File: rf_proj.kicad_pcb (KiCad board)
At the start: 2 copper layers, 85 parts, among them IC1 ATMEGA328P-A, P2 USB_OTG, P3 BNC, Q1 2N3904, SW1 SW_PUSH, U1 Si5351A_3, U2 CH340, U3 74AC74, U4 74CBTLV3253, U5 TLV2464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

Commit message: Layout verbessert.
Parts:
- removed Y1: 25MHZ, Crystals:Crystal_HC49-SD_SMD
- removed Y2: 12MHZ, Crystals:Crystal_HC49-SD_SMD
- removed Y3: 16MHZ, Crystals:Crystal_HC49-SD_SMD
- added C30: C_Small, Capacitors_SMD:C_0603_HandSoldering, F.Cu at (50.2, 96.5)
- added C31: C_Small, Capacitors_SMD:C_0603_HandSoldering, F.Cu at (50.2, 98.4)
- added C32: C_Small, Capacitors_SMD:C_0603_HandSoldering, F.Cu at (50.2, 102.2)
- added C33: C_Small, Capacitors_SMD:C_0603_HandSoldering, F.Cu at (50.2, 100.3)
- added C35: 10uF, Capacitors_SMD:C_0805_HandSoldering, F.Cu at (140.9, 113.8)
- added C36: 0.1uF, Capacitors_SMD:C_0603_HandSoldering, F.Cu at (145.8, 113.6)
- added CON1: AVR-ISP-6, Pin_Headers:Pin_Header_Straight_2x03, F.Cu at (268.0, 89.5)
- added D1: Led_Small, LEDs:LED_0603, F.Cu at (247.8, 84.5)
- added D2: Led_Small, LEDs:LED_0603, F.Cu at (247.8, 86.4)
- added D3: Led_Small, LEDs:LED_0603, F.Cu at (247.8, 88.3)
- added D4: Led_Small, LEDs:LED_0603, F.Cu at (247.8, 90.2)
- added D5: Led_Small, LEDs:LED_0603, F.Cu at (304.9, 66.7)
- added L8: INDUCTOR, Choke_SMD:Choke_SMD_1206_Handsoldering, F.Cu at (134.4, 114.3)
- added L9: INDUCTOR, Choke_SMD:Choke_SMD_1206_Handsoldering, F.Cu at (134.4, 121.4)
- added R32: 470, Resistors_SMD:R_0603_HandSoldering, F.Cu at (251.3, 84.5)
- added R33: 470, Resistors_SMD:R_0603_HandSoldering, F.Cu at (251.3, 86.4)
- added R34: 470, Resistors_SMD:R_0603_HandSoldering, F.Cu at (251.3, 88.3)
- added R35: 470, Resistors_SMD:R_0603_HandSoldering, F.Cu at (251.3, 90.2)
- added R36: 470, Resistors_SMD:R_0603_HandSoldering, F.Cu at (304.8, 69.2)
- added R37: 390, Resistors_SMD:R_0603_HandSoldering, F.Cu at (54.8, 103.5)
- added R38: R, Resistors_SMD:R_0603_HandSoldering, F.Cu at (140.6, 119.9)
- added T1: TRANSFO, rf-proj:RF-ProjTransformer, F.Cu at (34.9, 73.7)
- added X3: 25MHz, Crystals:Crystal_SMD_2520_4Pads, F.Cu at (214.3, 37.0)
- C34: footprint Resistors_SMD:R_0603_HandSoldering -> Capacitors_SMD:C_0603_HandSoldering
- moved X1 225.9 mm to (299.1, 84.5)
- moved SW1 176.1 mm to (315.0, 72.4)
- moved U2 176.1 mm to (297.2, 76.2)
- moved P2 176.1 mm to (297.8, 67.9)
- moved X2 163.6 mm to (247.0, 78.7)
- moved R6 133.7 mm to (23.8, 89.3), turned to 180 degrees
- moved U7 132.2 mm to (195.6, 128.5)
- moved C15 130.9 mm to (28.9, 91.2), turned to 90 degrees
- moved C11 126.6 mm to (252.7, 78.4), turned to 270 degrees
- moved IC1 125.0 mm to (260.4, 76.4)
- moved R5 122.6 mm to (28.9, 95.7), turned to 270 degrees
- moved R7 119.1 mm to (30.8, 95.7), turned to 90 degrees
- moved R4 115.8 mm to (28.4, 88.0), turned to 180 degrees
- moved R8 114.9 mm to (23.2, 92.9), turned to 90 degrees
- moved C20 106.4 mm to (30.8, 91.2), turned to 270 degrees
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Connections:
- C10 pad 2: GND -> GNDA
- C18 pad 2: GND -> GNDA
- C22 pad 2: GND -> GNDA
- C27 pad 2: GND -> GNDA
- C28 pad 2: GND -> GNDA
- C6 pad 2: GND -> GNDA
- C7 pad 2: GND -> GNDA
- C9 pad 2: GND -> GNDA
- R22 pad 1: GND -> GNDA
- R30 pad 1: GND -> GNDA
- R6 pad 2: GND -> GNDA
- R8 pad 2: GND -> GNDA
- U4 pad 8: GND -> GNDA
- U4 pad 9: Net-(U4-Pad9) -> GNDA
- U5 pad 11: GND -> GNDA
- U5 pad 12: /IN_D -> (no net)
- U5 pad 13: Net-(R19-Pad1) -> (no net)
- U5 pad 14: Net-(R24-Pad1) -> (no net)
- U6 pad 11: GND -> GNDA
- U6 pad 12: (no net) -> Net-(C24-Pad1)
- U6 pad 13: (no net) -> /V_REF
- U6 pad 14: (no net) -> /V_REF
- U6 pad 5: Net-(C24-Pad1) -> /IN_D
- U6 pad 6: /V_REF -> Net-(R19-Pad1)
- U6 pad 7: /V_REF -> Net-(R24-Pad1)
- U7 pad 1: GND -> GNDA
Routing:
- net Net-(L5-Pad1): track 0.00 -> 12.4 mm
- net Net-(R27-Pad1): track 0.00 -> 9.21 mm
- net Net-(C15-Pad1): track 0.00 -> 8.52 mm
- net Net-(R19-Pad1): track 0.00 -> 6.91 mm
- net Net-(R19-Pad2): track 0.00 -> 6.77 mm
- net Net-(R23-Pad1): track 0.00 -> 4.66 mm
- net Net-(C29-Pad1): track 0.00 -> 4.21 mm
- net Net-(R26-Pad1): track 0.00 -> 3.97 mm
- net /V_REF: track 0.00 -> 2.94 mm
- net GNDA: track 0.00 -> 2.73 mm
- net Net-(C15-Pad2): track 0.00 -> 2.49 mm
- net Net-(Q1-Pad1): track 0.00 -> 2.25 mm
- net Net-(R24-Pad1): track 0.00 -> 2.15 mm

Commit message: Routing und Fehlerkorrekturen im Schaltplan
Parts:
- added C37: 10uF, Capacitors_SMD:C_0805_HandSoldering, F.Cu at (102.2, 116.8)
- added C38: 0.1uF, Capacitors_SMD:C_0603_HandSoldering, F.Cu at (99.1, 118.1)
- added C39: 10uF, Capacitors_SMD:C_0805_HandSoldering, F.Cu at (128.9, 110.5)
- added C40: 0.1uF, Capacitors_SMD:C_0603_HandSoldering, F.Cu at (127.6, 107.3)
- added C41: 1uF, Capacitors_SMD:C_0603_HandSoldering, F.Cu at (172.1, 89.2)
- added J1: JACK_TRS_6PINS, Connect:PINHEAD1-6, F.Cu at (141.0, 108.0)
- added L10: INDUCTOR, rf-proj:L_0805_HandSoldering, F.Cu at (102.2, 119.4)
- added L11: INDUCTOR, rf-proj:L_0805_HandSoldering, F.Cu at (126.4, 110.5)
- added R39: R, Resistors_SMD:R_0603_HandSoldering, F.Cu at (102.2, 121.3)
- added R40: R, Resistors_SMD:R_0603_HandSoldering, F.Cu at (124.5, 110.5)
- L1, L2, L3, L4, L5, L6, L7, L8, L9: footprint Choke_SMD:Choke_SMD_1206_Handsoldering -> rf-proj:L_0805_HandSoldering
- moved SW1 146.9 mm to (177.8, 125.1), turned to 180 degrees
- moved X1 135.3 mm to (163.8, 81.2), turned to 270 degrees
- moved U2 125.2 mm to (172.1, 80.6), turned to 180 degrees
- moved R36 124.1 mm to (180.8, 74.3)
- moved D5 124.1 mm to (181.0, 72.4)
- moved L7 121.1 mm to (184.8, 154.3), turned to 180 degrees
- moved P2 118.1 mm to (180.4, 80.0), turned to 90 degrees
- moved R20 108.9 mm to (108.6, 119.4), turned to 180 degrees
- moved U3 99.6 mm to (155.2, 125.8)
- moved U1 99.5 mm to (162.6, 125.4), turned to 180 degrees
- moved X3 99.1 mm to (168.9, 125.1)
- moved R14 96.4 mm to (116.2, 116.2), turned to 270 degrees
- moved C27 93.3 mm to (197.5, 149.2)
- moved C11 93.2 mm to (160.7, 92.7), turned to 0 degrees
- moved IC1 92.0 mm to (170.8, 97.2)
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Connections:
- C16 pad 2: GND -> GNDA
- C18 pad 1: /3.3A -> Net-(C18-Pad1)
- C19 pad 2: GND -> GNDA
- C22 pad 1: /3.3A -> Net-(C18-Pad1)
- C24 pad 2: GND -> GNDA
- C34 pad 2: GND -> GNDA
- P2 pad 6: Net-(P2-Pad6) -> GND
- R21 pad 1: GND -> GNDA
- R7 pad 1: /3.3A -> Net-(C38-Pad1)
- U2 pad 13: Net-(U2-Pad13) -> /DTR
- U4 pad 1: Net-(U4-Pad1) -> GNDA
- U4 pad 15: Net-(U4-Pad15) -> Net-(C19-Pad1)
- U5 pad 12: (no net) -> Net-(C24-Pad1)
- U5 pad 13: (no net) -> /V_REF
- U5 pad 14: (no net) -> /V_REF
- U5 pad 4: /3.3A -> Net-(C18-Pad1)
- U6 pad 12: Net-(C24-Pad1) -> GNDA
- U6 pad 13: /V_REF -> GNDA
- U6 pad 14: /V_REF -> Net-(U6-Pad14)
- U6 pad 4: /3.3A -> Net-(C18-Pad1)
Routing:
- net GNDA: track 2.73 -> 77.8 mm, vias 0 -> 5
- net GND: track 0.00 -> 69.7 mm
- net /S0: track 0.00 -> 55.3 mm, vias 0 -> 3
- net /S1: track 0.00 -> 50.9 mm, vias 0 -> 2
- net /RESET: track 0.00 -> 41.3 mm
- net /S_Mixer: track 0.00 -> 41.2 mm, vias 0 -> 3
- net /3.3A: track 0.00 -> 35.8 mm, vias 0 -> 2
- net Net-(C18-Pad1): track 0.00 -> 35.4 mm, vias 0 -> 5
- net Net-(C38-Pad1): track 0.00 -> 30.9 mm
- net +3V3: track 0.00 -> 30.4 mm
- net /V_REF: track 2.94 -> 29.2 mm
- net Net-(C24-Pad1): track 0.00 -> 22.9 mm, vias 0 -> 2
- net Net-(C2-Pad1): track 0.00 -> 22.1 mm
- net /IN_C: track 0.00 -> 21.1 mm
- net /IN_D: track 0.00 -> 20.8 mm
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- added copper zone on B.Cu, net GND
- added copper zone on F.Cu, net GND
- added copper zone on B.Cu, net GNDA
- added copper zone on F.Cu, net GNDA
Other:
- net class Default: via_dia 0.8 -> 1
- rule trace_min: 0.2 -> 0.25
- rule via_min_drill: 0.3 -> 0.4
- rule via_min_size: 0.4 -> 1

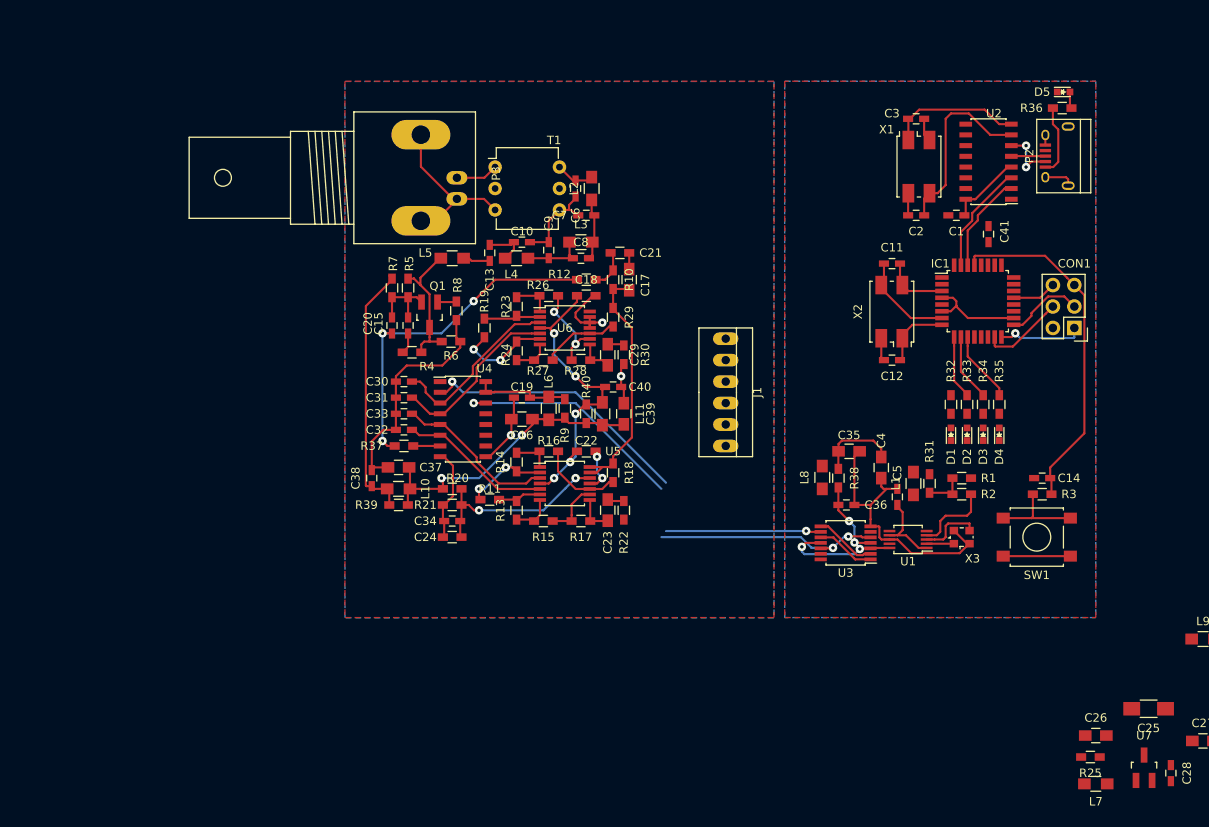
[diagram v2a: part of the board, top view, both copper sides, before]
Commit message: Footprints angepasst und Layout bearbeitet
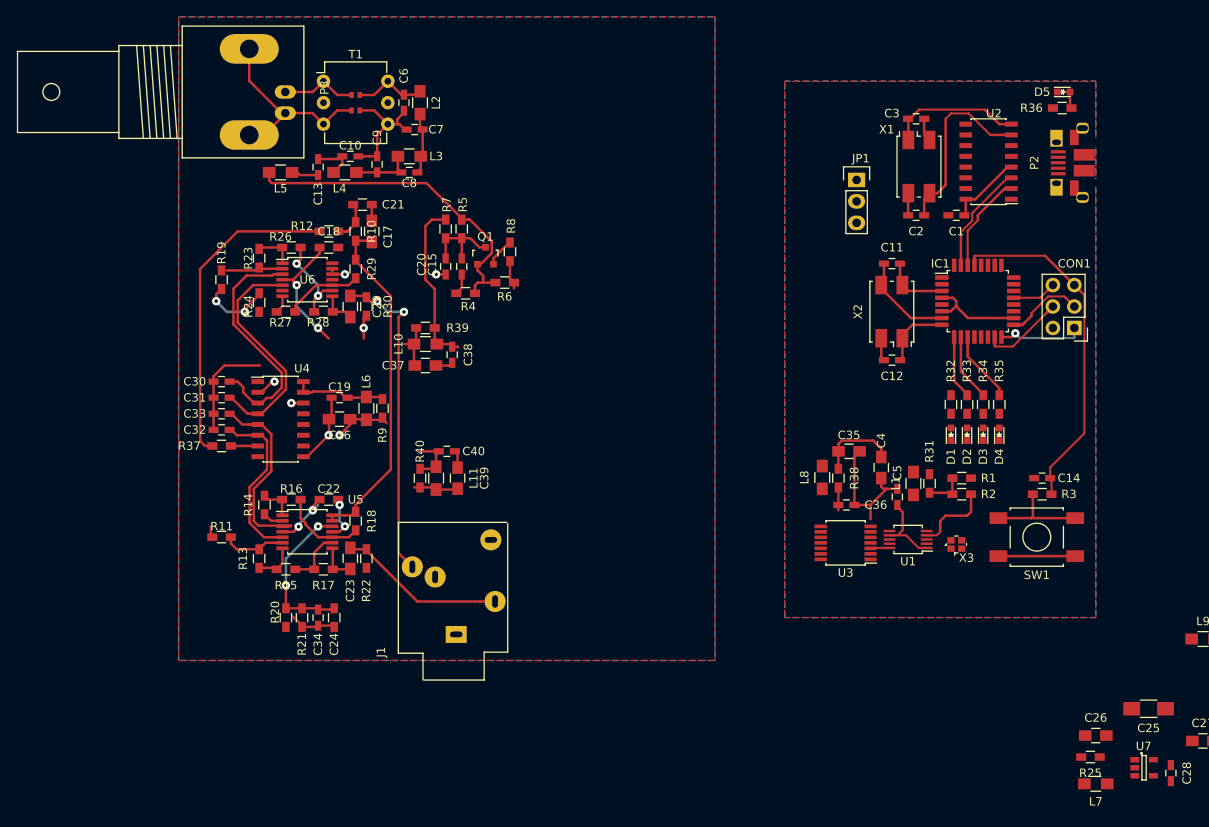
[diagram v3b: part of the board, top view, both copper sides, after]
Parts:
- removed C41: 1uF, Capacitors_SMD:C_0603_HandSoldering
- added JP1: JUMPER3, Pin_Headers:Pin_Header_Straight_1x03, F.Cu at (156.5, 82.8)
- J1: value JACK_TRS_6PINS -> EBS_35; footprint Connect:PINHEAD1-6 -> rf-proj:EBS_35
- P2: footprint Connect:USB_Micro-B -> rf-proj:USB_Micro-B
- Q1: value 2N3904 -> BC849; footprint TO_SOT_Packages_SMD:SOT-23_Handsoldering -> TO_SOT_Packages_SMD:SOT-23
- SW1: footprint Buttons_Switches_SMD:SW_SPST_B3S-1000 -> rf-proj:TASTER_9315
- U7: value AP1117D33 -> MIC5504-3.3; footprint TO_SOT_Packages_SMD:SOT-23_Handsoldering -> TO_SOT_Packages_SMD:SOT-23-5
- X3: footprint Crystals:Crystal_SMD_2520_4Pads -> rf-proj:Crystal_SMD_2016_4Pads
- moved J1 46.7 mm to (109.1, 142.0), turned to 90 degrees
- moved R11 32.1 mm to (81.3, 125.1)
- moved R19 31.6 mm to (81.3, 94.6)
- moved C21 31.0 mm to (98.0, 85.7)
- moved C23 31.0 mm to (96.5, 127.6)
- moved C29 31.0 mm to (96.5, 97.8)
- moved R10 31.0 mm to (97.2, 88.9)
- moved R13 31.0 mm to (85.7, 127.6)
- moved R16 31.0 mm to (89.5, 120.7)
- moved R17 31.0 mm to (93.3, 128.9)
- moved R18 31.0 mm to (97.2, 123.2)
- moved R22 31.0 mm to (98.4, 127.6)
- moved R23 31.0 mm to (85.7, 92.1)
- moved R24 31.0 mm to (85.7, 97.3)
- moved R26 31.0 mm to (89.5, 90.8)
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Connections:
- C14 pad 1: /RESET -> Net-(C14-Pad1)
- C14 pad 2: GND -> Net-(C14-Pad2)
- C17 pad 2: GND -> GNDA
- C21 pad 2: GND -> GNDA
- C36 pad 1: Net-(C36-Pad1) -> VCC
- L8 pad 1: Net-(C36-Pad1) -> VCC
- Q1 pad 1: Net-(Q1-Pad1) -> Net-(L5-Pad1)
- Q1 pad 2: Net-(C15-Pad1) -> Net-(Q1-Pad2)
- Q1 pad 3: Net-(L5-Pad1) -> Net-(C15-Pad1)
- R38 pad 2: Net-(C36-Pad1) -> VCC
- R8 pad 1: Net-(Q1-Pad1) -> Net-(Q1-Pad2)
- U3 pad 10: /CLK_RST -> VCC
- U3 pad 13: Net-(U3-Pad13) -> /CLK_RST
- U3 pad 4: Net-(C36-Pad1) -> VCC
- U7 pad 1: GNDA -> Net-(C26-Pad1)
- U7 pad 2: /3.3A -> GNDA
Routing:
- net /S0: track 55.3 -> 1.43 mm, vias 3 -> 1
- net /S1: track 50.9 -> 3.24 mm, vias 2 -> 1
- net /OUT_Q: track 1.97 -> 38.3 mm, vias 0 -> 2
- net GND: track 69.7 -> 45.1 mm
- net Net-(L5-Pad1): track 16.6 -> 39.9 mm
- net /OUT_I: track 1.98 -> 19.9 mm
- net /3.3A: track 35.8 -> 18.8 mm, vias 2 -> 1
- net GNDA: track 77.8 -> 61.3 mm
- net /V_REF: track 29.2 -> 41.1 mm
- net /CLK: track 13.8 -> 2.27 mm, vias 2 -> 0
- net Net-(C38-Pad1): track 30.9 -> 19.9 mm
- net Net-(C36-Pad1): track 9.23 -> 0.00 mm, vias 2 -> 0
- net Net-(C25-Pad1): track 8.42 -> 0.00 mm
- net /IN_C: track 21.1 -> 28.9 mm
- net Net-(U1-Pad3): track 7.48 -> 0.00 mm
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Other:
- net class Default: trace_width 0.25 -> 0.3
- rule pad_to_mask_clearance: 0 -> 0.2
- rule trace_min: 0.25 -> 0.3

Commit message: Layout fertig
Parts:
- removed C40: 0.1uF, Capacitors_SMD:C_0603_HandSoldering
- added C41: 10uF, Capacitors_SMD:C_0805_HandSoldering, F.Cu at (106.7, 87.6)
- added L12: INDUCTOR, rf-proj:L_0805_HandSoldering, F.Cu at (103.5, 91.4)
- added R41: R, Resistors_SMD:R_0603_HandSoldering, F.Cu at (101.6, 91.6)
- moved C27 118.3 mm to (108.2, 71.7), turned to 90 degrees
- moved C28 116.6 mm to (110.1, 71.7), turned to 90 degrees
- moved U7 112.0 mm to (112.9, 71.7), turned to 180 degrees
- moved L7 107.5 mm to (117.2, 70.7), turned to 0 degrees
- moved R25 103.2 mm to (117.2, 72.6), turned to 0 degrees
- moved L9 100.3 mm to (117.2, 77.1)
- moved C26 100.3 mm to (117.2, 74.5)
- moved C25 99.3 mm to (123.5, 72.6), turned to 270 degrees
- moved SW1 59.9 mm to (128.3, 91.4), turned to 0 degrees
- moved R3 47.7 mm to (138.4, 94.0), turned to 90 degrees
- moved C14 45.1 mm to (140.3, 94.0), turned to 90 degrees
- moved C3 34.0 mm to (129.9, 70.4)
- moved X1 34.0 mm to (130.2, 76.0)
- moved C2 34.0 mm to (129.9, 81.8)
- moved IC1 33.4 mm to (137.8, 102.2)
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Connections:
- C14 pad 1: Net-(C14-Pad1) -> /RESET
- C22 pad 1: Net-(C18-Pad1) -> Net-(C22-Pad1)
- U6 pad 4: Net-(C18-Pad1) -> Net-(C22-Pad1)
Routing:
- net /3.3A: track 18.8 -> 119.4 mm, vias 1 -> 2
- net +3V3: track 30.4 -> 101.5 mm, vias 0 -> 2
- net /S0: track 1.43 -> 56.7 mm, vias 1 -> 3
- net /CLK_RST: track 0.00 -> 52.5 mm, vias 0 -> 2
- net GND: track 45.1 -> 93.1 mm, vias 0 -> 1
- net /S1: track 3.24 -> 50.4 mm, vias 1 -> 2
- net /SDA: track 0.55 -> 43.5 mm, vias 0 -> 2
- net Net-(C25-Pad1): track 0.00 -> 40.4 mm
- net /SCL: track 9.22 -> 43.7 mm, vias 0 -> 2
- net Net-(L5-Pad1): track 39.9 -> 16.2 mm
- net VCC: track 2.71 -> 22.9 mm
- net /RESET: track 38.1 -> 18.6 mm
- net GNDA: track 61.3 -> 79.3 mm, vias 5 -> 7
- net Net-(IC1-Pad2): track 0.00 -> 17.5 mm, vias 0 -> 2
- net /S_Mixer: track 39.2 -> 55.5 mm, vias 1 -> 0
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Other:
- board outline added: 76.2 x 76.2 mm
- rule pad_to_mask_clearance: 0.2 -> 0.15

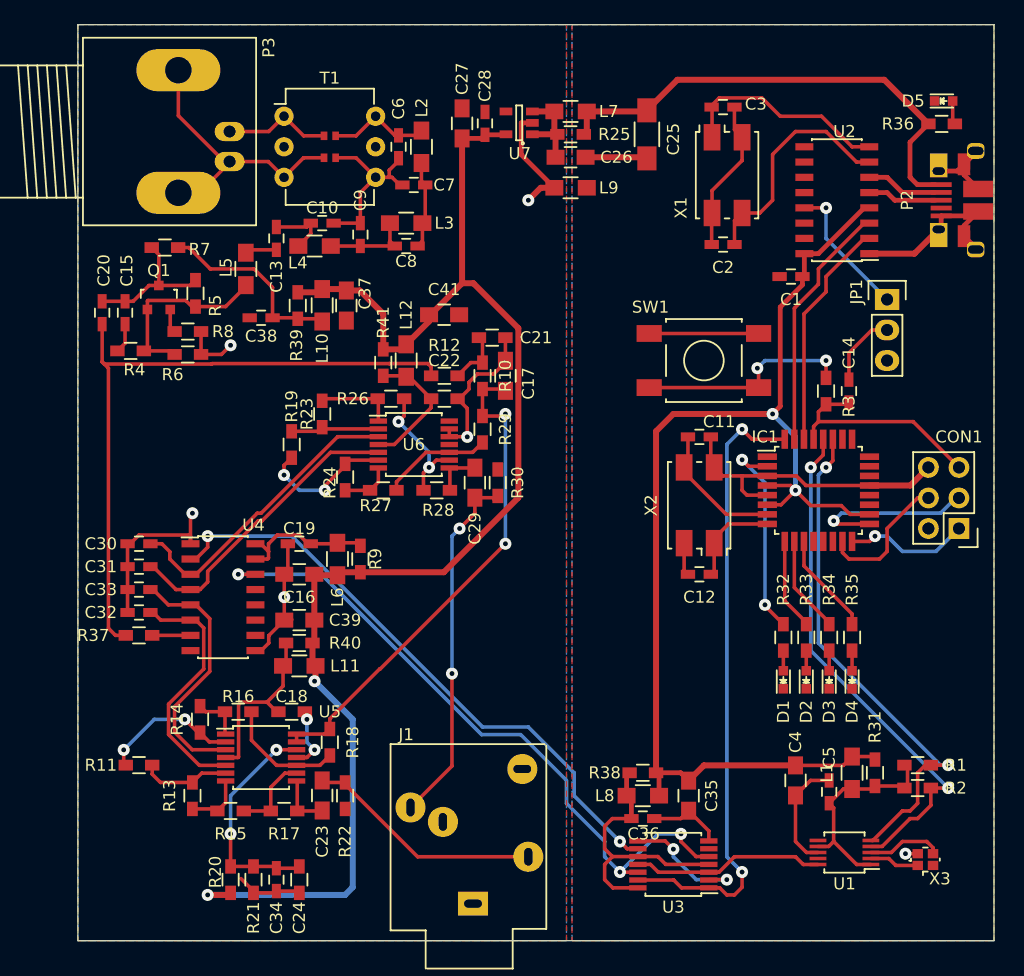
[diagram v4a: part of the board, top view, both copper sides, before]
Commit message: Diverse Layout-Korrekturen und -Verbesserungen
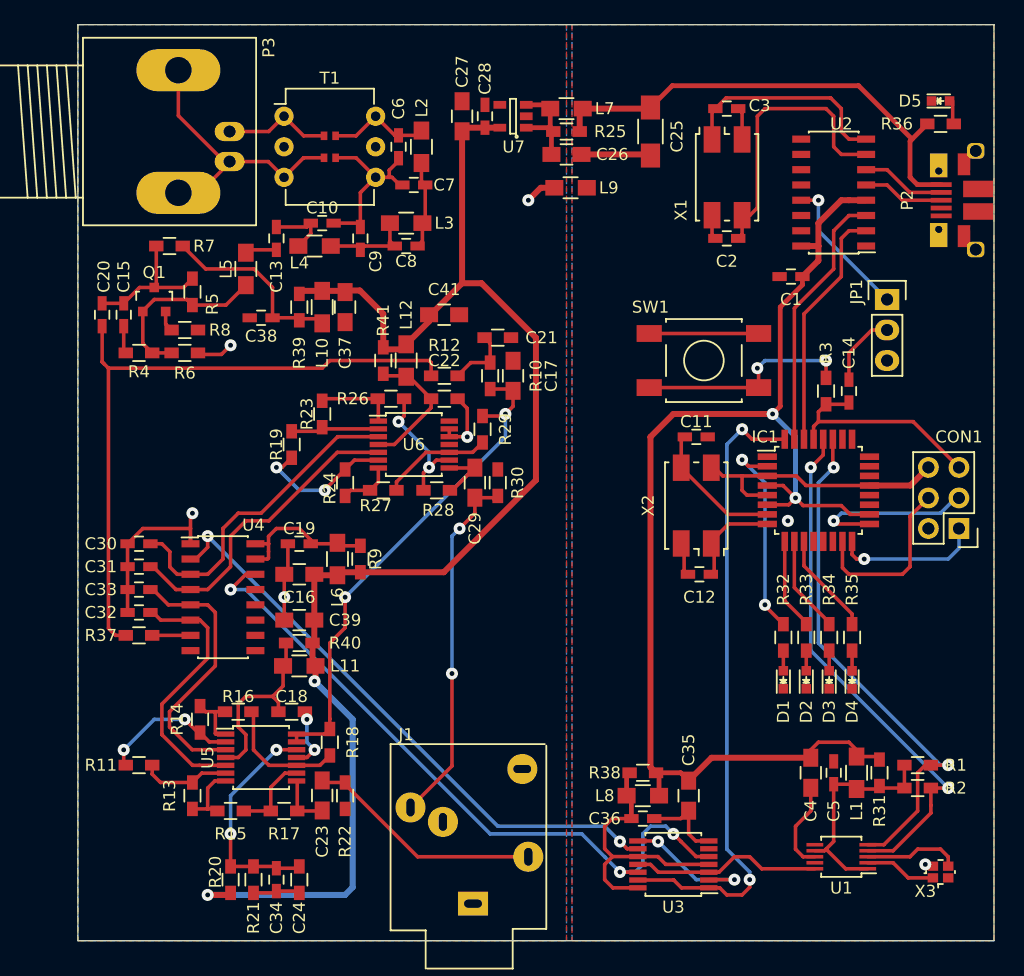
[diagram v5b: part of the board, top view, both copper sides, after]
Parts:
- P2: footprint rf-proj:USB_Micro-B -> USB_Micro-B
- moved X3 1.63 mm to (148.0, 134.0)
- moved C5 1.63 mm to (139.1, 125.7)
- moved C4 1.42 mm to (137.2, 125.7)
- moved U7 0.75 mm to (112.4, 71.1)
- moved R4 0.71 mm to (81.3, 90.8)
- moved U2 0.69 mm to (139.1, 77.5)
- moved C17 0.63 mm to (112.4, 92.7)
- moved R10 0.63 mm to (110.5, 92.7)
- moved C2 0.59 mm to (130.2, 81.3)
- moved C27 0.59 mm to (108.2, 71.1)
- moved C28 0.59 mm to (110.1, 71.1)
- moved C21 0.47 mm to (111.1, 89.5)
- moved R24 0.46 mm to (98.4, 101.6)
- moved U1 0.44 mm to (139.7, 132.7)
- moved Q1 0.42 mm to (82.5, 86.4)
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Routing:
- net GND: track 93.1 -> 61.1 mm
- net GNDA: track 79.3 -> 57.8 mm
- net +3V3: track 101.5 -> 106.1 mm
- net Net-(C2-Pad1): track 19.6 -> 23.6 mm
- net Net-(CON1-Pad4): track 11.5 -> 14.7 mm
- net Net-(U1-Pad2): track 3.75 -> 5.94 mm
- net Net-(CON1-Pad1): track 10.1 -> 12.2 mm
- net /IN_C: track 25.1 -> 27.0 mm
- net Net-(U1-Pad3): track 6.26 -> 8.00 mm
- net /IN_B: track 21.4 -> 22.7 mm
- net /IN_A: track 20.9 -> 22.1 mm
- net /TXD: track 19.2 -> 20.3 mm
- net /S1: track 50.4 -> 49.3 mm
- net /S0: track 56.7 -> 57.7 mm
- net Net-(C29-Pad1): track 3.95 -> 5.00 mm
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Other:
- net class Default: clearance 0.2 -> 0.25
- rule trace_clearance: 0.2 -> 0.25

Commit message: Weitere Fehlerkorrekturen
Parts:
- moved T1 0.63 mm to (97.2, 73.0)
- moved L9 0.50 mm to (116.8, 76.7)
- moved C27 0.21 mm to (108.0, 71.1)
- moved C28 0.21 mm to (109.9, 71.1)
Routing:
- net GND: track 61.1 -> 23.5 mm
- net GNDA: track 57.8 -> 34.9 mm, vias 7 -> 6
- net /3.3A: track 119.9 -> 114.2 mm
- net Net-(C5-Pad1): track 18.9 -> 22.9 mm
- net /OUT_Q: track 30.4 -> 32.9 mm
- net Net-(R19-Pad1): track 11.9 -> 13.7 mm
- net /CLK_RST: track 53.4 -> 54.6 mm
- net Net-(C25-Pad1): track 39.9 -> 40.8 mm
- net Net-(C6-Pad1): track 8.64 -> 9.41 mm
- net (no net): vias 1 -> 0
